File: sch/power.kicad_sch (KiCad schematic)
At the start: 3 parts

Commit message: Memory Module
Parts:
- removed C4: ~, Capacitor_THT:CP_Radial_D4.0mm_P1.50mm, symbol Device:C_Polarized_Small
- added C1: (no value), symbol Device:C_Polarized_Small
- added PWREG2: (no value), symbol Regulator_Linear:LT1962-5
- renumbered UPWR1 to PWREG1
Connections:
- net 5V: now also PWREG2.1 (OUT)
- net BOARD_IN: now also C3.1, PWREG1.1 (VIN), C1.1, PWREG2.8 (IN)
- net GND: now also C3.2, C1.2, PWREG2.4 (GND)
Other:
- moved on the sheet: C3, PWREG1
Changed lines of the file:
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@@
 (kicad_sch (version 20211123) (generator eeschema)
   (paper "A4")
-  (hierarchical_label "BOARD_IN" (shape input) (at 58.42 66.04 180)
+  (junction (at 139.7 114.3) (diameter 0) (color 0 0 0 0)
+  )
+  (junction (at 139.7 73.66) (diameter 0) (color 0 0 0 0)
+  )
+  (wire (pts (xy 139.7 73.66) (xy 139.7 78.74))
+    (stroke (width 0) (type default) (color 0 0 0 0))
+  )
+  (wire (pts (xy 177.8 114.3) (xy 165.1 114.3))
+    (stroke (width 0) (type default) (color 0 0 0 0))
+  )
+  (wire (pts (xy 139.7 114.3) (xy 144.78 114.3))
+    (stroke (width 0) (type default) (color 0 0 0 0))
+  )
+  (wire (pts (xy 127 73.66) (xy 139.7 73.66))
+    (stroke (width 0) (type default) (color 0 0 0 0))
+  )
+  (wire (pts (xy 139.7 114.3) (xy 139.7 119.38))
+    (stroke (width 0) (type default) (color 0 0 0 0))
+  )
+  (wire (pts (xy 127 114.3) (xy 139.7 114.3))
+    (stroke (width 0) (type default) (color 0 0 0 0))
+  )
+  (wire (pts (xy 139.7 73.66) (xy 144.78 73.66))
+    (stroke (width 0) (type default) (color 0 0 0 0))
+  )
+  (hierarchical_label "BOARD_IN" (shape input) (at 127 73.66 180)
     (effects (font (size 1.27 1.27)) (justify right))
   )
-  (hierarchical_label "3.3V" (shape output) (at 191.77 86.36 0)
+  (hierarchical_label "3.3V" (shape output) (at 191.77 83.82 0)
     (effects (font (size 1.27 1.27)) (justify left))
   )
-  (hierarchical_label "12V" (shape output) (at 191.77 78.74 0)
+  (hierarchical_label "12V" (shape output) (at 191.77 76.2 0)
     (effects (font (size 1.27 1.27)) (justify left))
   )
-  (hierarchical_label "5V" (shape output) (at 191.77 82.55 0)
+  (hierarchical_label "5V" (shape output) (at 177.8 114.3 0)
     (effects (font (size 1.27 1.27)) (justify left))
   )
-  (symbol (lib_id "Device:C_Polarized_Small") (at 86.36 68.58 0) (unit 1)
+  (hierarchical_label "BOARD_IN" (shape input) (at 127 114.3 180)
+    (effects (font (size 1.27 1.27)) (justify right))
+  )
+  (symbol (lib_id "power:GND") (at 154.94 127 0) (unit 1)
     (in_bom yes) (on_board yes) (fields_autoplaced)
-    (property "Reference" "C4" (id 0) (at 88.9 66.7638 0)
+    (property "Reference" "#PWR0117" (id 0) (at 154.94 133.35 0)
+      (effects (font (size 1.27 1.27)) hide)
+    )
+    (property "Value" "GND" (id 1) (at 154.94 132.08 0))
+    (property "Footprint" "" (id 2) (at 154.94 127 0)
+      (effects (font (size 1.27 1.27)) hide)
+    )
+    (property "Datasheet" "" (id 3) (at 154.94 127 0)
+      (effects (font (size 1.27 1.27)) hide)
+    )
+    (pin "1")
+  )
+  (symbol (lib_id "Device:C_Polarized_Small") (at 139.7 121.92 0) (unit 1)
+    (in_bom yes) (on_board yes)
+    (property "Reference" "C1" (id 0) (at 134.62 120.65 0)
       (effects (font (size 1.27 1.27)) (justify left))
     )
-    (property "Value" "~" (id 1) (at 88.9 69.3038 0)
+    (property "Value" "" (id 1) (at 119.38 123.19 0)
       (effects (font (size 1.27 1.27)) (justify left))
     )
-    (property "Footprint" "Capacitor_THT:CP_Radial_D4.0mm_P1.50mm" (id 2) (at 86.36 68.58 0)
+    (property "Footprint" "" (id 2) (at 139.7 121.92 0)
       (effects (font (size 1.27 1.27)) hide)
     )
-    (property "Datasheet" "~" (id 3) (at 86.36 68.58 0)
+    (property "Datasheet" "~" (id 3) (at 139.7 121.92 0)
       (effects (font (size 1.27 1.27)) hide)
     )
@@
     (pin "2")
   )
-  (symbol (lib_id "power:GND") (at 105.41 82.55 0) (unit 1)
+  (symbol (lib_id "power:GND") (at 154.94 83.82 0) (unit 1)
     (in_bom yes) (on_board yes) (fields_autoplaced)
-    (property "Reference" "#PWR01" (id 0) (at 105.41 88.9 0)
+    (property "Reference" "#PWR01" (id 0) (at 154.94 90.17 0)
       (effects (font (size 1.27 1.27)) hide)
     )
-    (property "Value" "GND" (id 1) (at 105.41 87.63 0))
-    (property "Footprint" "" (id 2) (at 105.41 82.55 0)
+    (property "Value" "GND" (id 1) (at 154.94 88.9 0))
+    (property "Footprint" "" (id 2) (at 154.94 83.82 0)
       (effects (font (size 1.27 1.27)) hide)
     )
-    (property "Datasheet" "" (id 3) (at 105.41 82.55 0)
+    (property "Datasheet" "" (id 3) (at 154.94 83.82 0)
       (effects (font (size 1.27 1.27)) hide)
     )
     (pin "1")
   )
-  (symbol (lib_id "Regulator_Linear:LT1761-1.5") (at 105.41 74.93 0) (unit 1)
+  (symbol (lib_id "Regulator_Linear:LT1962-5") (at 154.94 119.38 0) (unit 1)
     (in_bom yes) (on_board yes) (fields_autoplaced)
-    (property "Reference" "UPWR1" (id 0) (at 105.41 64.77 0))
-    (property "Value" "LT1761-1.5" (id 1) (at 105.41 67.31 0))
-    (property "Footprint" "Package_TO_SOT_SMD:TSOT-23-5" (id 2) (at 105.41 66.675 0)
+    (property "Reference" "PWREG2" (id 0) (at 154.94 106.68 0))
+    (property "Value" "" (id 1) (at 154.94 109.22 0))
+    (property "Footprint" "" (id 2) (at 154.94 128.27 0)
       (effects (font (size 1.27 1.27)) hide)
     )
-    (property "Datasheet" "https://www.analog.com/media/en/technical-documentation/data-sheets/1761sff.pdf" (id 3) (at 105.41 74.93 0)
+    (property "Datasheet" "https://www.analog.com/media/en/technical-documentation/data-sheets/1962fb.pdf" (id 3) (at 154.94 133.35 0)
+      (effects (font (size 1.27 1.27)) hide)
+    )
+    (pin "1")
+    (pin "2")
+    (pin "3")
+    (pin "4")
+    (pin "5")
+    (pin "6")
+    (pin "7")
+    (pin "8")
+  )
+  (symbol (lib_id "Regulator_Linear:LT1761-1.5") (at 154.94 76.2 0) (unit 1)
+    (in_bom yes) (on_board yes) (fields_autoplaced)
+    (property "Reference" "PWREG1" (id 0) (at 154.94 66.04 0))
+    (property "Value" "LT1761-1.5" (id 1) (at 154.94 68.58 0))
+    (property "Footprint" "Package_TO_SOT_SMD:TSOT-23-5" (id 2) (at 154.94 67.945 0)
+      (effects (font (size 1.27 1.27)) hide)
+    )
+    (property "Datasheet" "https://www.analog.com/media/en/technical-documentation/data-sheets/1761sff.pdf" (id 3) (at 154.94 76.2 0)
       (effects (font (size 1.27 1.27)) hide)
     )
@@
     (pin "5")
   )
-  (symbol (lib_id "Device:C_Polarized_Small") (at 90.17 58.42 0) (unit 1)
+  (symbol (lib_id "power:GND") (at 139.7 124.46 0) (unit 1)
+    (in_bom yes) (on_board yes) (fields_autoplaced)
+    (property "Reference" "#PWR0118" (id 0) (at 139.7 130.81 0)
+      (effects (font (size 1.27 1.27)) hide)
+    )
+    (property "Value" "GND" (id 1) (at 139.7 129.54 0))
+    (property "Footprint" "" (id 2) (at 139.7 124.46 0)
+      (effects (font (size 1.27 1.27)) hide)
+    )
+    (property "Datasheet" "" (id 3) (at 139.7 124.46 0)
+      (effects (font (size 1.27 1.27)) hide)
+    )
+    (pin "1")
+  )
+  (symbol (lib_id "power:GND") (at 139.7 83.82 0) (unit 1)
+    (in_bom yes) (on_board yes) (fields_autoplaced)
+    (property "Reference" "#PWR0111" (id 0) (at 139.7 90.17 0)
+      (effects (font (size 1.27 1.27)) hide)
+    )
+    (property "Value" "GND" (id 1) (at 139.7 88.9 0))
+    (property "Footprint" "" (id 2) (at 139.7 83.82 0)
+      (effects (font (size 1.27 1.27)) hide)
+    )
+    (property "Datasheet" "" (id 3) (at 139.7 83.82 0)
+      (effects (font (size 1.27 1.27)) hide)
+    )
+    (pin "1")
+  )
+  (symbol (lib_id "Device:C_Polarized_Small") (at 139.7 81.28 0) (unit 1)
     (in_bom yes) (on_board yes)
-    (property "Reference" "C3" (id 0) (at 92.71 56.6038 0)
+    (property "Reference" "C3" (id 0) (at 134.62 80.01 0)
       (effects (font (size 1.27 1.27)) (justify left))
     )
-    (property "Value" "C_Polarized_Small" (id 1) (at 92.71 59.1438 0)
+    (property "Value" "C_Polarized_Small" (id 1) (at 119.38 82.55 0)
       (effects (font (size 1.27 1.27)) (justify left))
     )
-    (property "Footprint" "Capacitor_THT:CP_Radial_D5.0mm_P2.00mm" (id 2) (at 90.17 58.42 0)
+    (property "Footprint" "Capacitor_THT:CP_Radial_D5.0mm_P2.00mm" (id 2) (at 139.7 81.28 0)
       (effects (font (size 1.27 1.27)) hide)
     )
-    (property "Datasheet" "~" (id 3) (at 90.17 58.42 0)
+    (property "Datasheet" "~" (id 3) (at 139.7 81.28 0)
       (effects (font (size 1.27 1.27)) hide)
     )

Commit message: Bus control
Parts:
- removed C3: C_Polarized_Small, Capacitor_THT:CP_Radial_D5.0mm_P2.00mm, symbol Device:C_Polarized_Small
- removed PWREG1: LT1761-1.5, Package_TO_SOT_SMD:TSOT-23-5, symbol Regulator_Linear:LT1761-1.5
- added C11: (no value), symbol Device:C
- added SW1: (no value), symbol Switch:SW_Push
- added U6: (no value), symbol Power_Supervisor:MAX811MEUS-T
- C1: footprint (none) -> Capacitor_THT:CP_Radial_D5.0mm_P2.00mm
- PWREG2: value (none) -> LT1962-5; footprint (none) -> Package_SO:MSOP-8_3x3mm_P0.65mm
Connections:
- net 5V: now also U6.4 (VCC)
- net GND: now also C11.2, SW1.1, U6.1 (GND)
- net BOARD_IN renamed PWR
- new net: C11.1, SW1.2, U6.3 (~{MR})
- new net RST: U6.2 (~{RESET})
- no-connect marks 0 -> 2
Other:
- moved on the sheet: C1, PWREG2

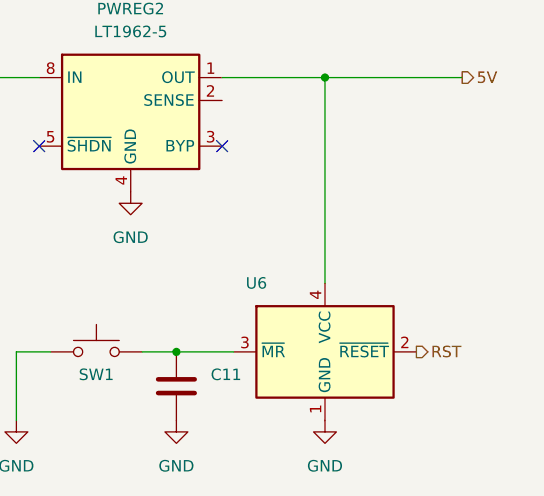
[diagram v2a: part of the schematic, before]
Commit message: New address decoder
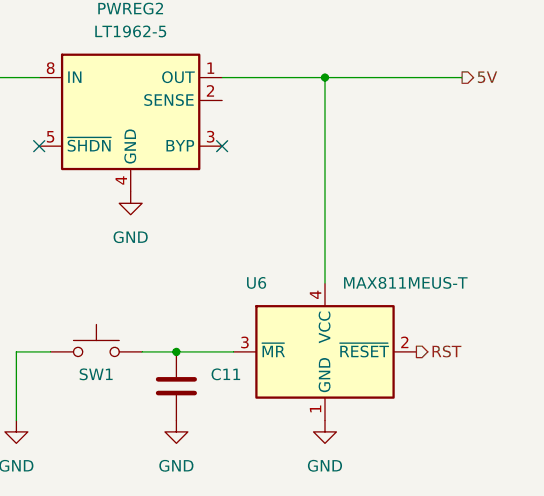
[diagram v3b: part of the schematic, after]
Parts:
- C1: footprint Capacitor_THT:CP_Radial_D5.0mm_P2.00mm -> (none)
- U6: value (none) -> MAX811MEUS-T; footprint (none) -> Package_TO_SOT_SMD:SOT-143
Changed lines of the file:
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@@
       (effects (font (size 1.27 1.27)) (justify right))
     )
-    (property "Footprint" "Capacitor_THT:CP_Radial_D5.0mm_P2.00mm" (id 2) (at 114.3 91.44 0)
+    (property "Footprint" "" (id 2) (at 114.3 91.44 0)
       (effects (font (size 1.27 1.27)) hide)
     )
@@
     (in_bom yes) (on_board yes)
     (property "Reference" "U6" (id 0) (at 148.59 104.14 0))
-    (property "Value" "" (id 1) (at 165.1 104.14 0))
-    (property "Footprint" "" (id 2) (at 158.75 119.38 0)
+    (property "Value" "MAX811MEUS-T" (id 1) (at 165.1 104.14 0))
+    (property "Footprint" "Package_TO_SOT_SMD:SOT-143" (id 2) (at 158.75 119.38 0)
       (effects (font (size 1.27 1.27)) (justify left) hide)
     )

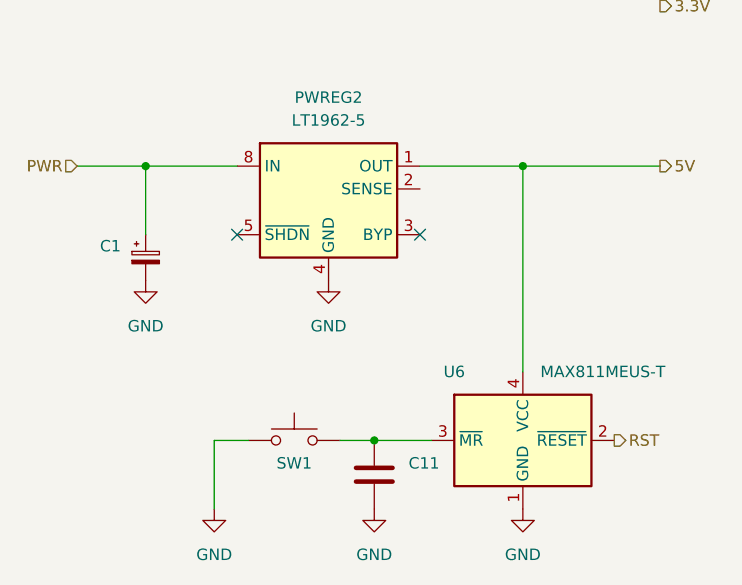
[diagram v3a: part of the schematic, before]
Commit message: Board layout, addr bus
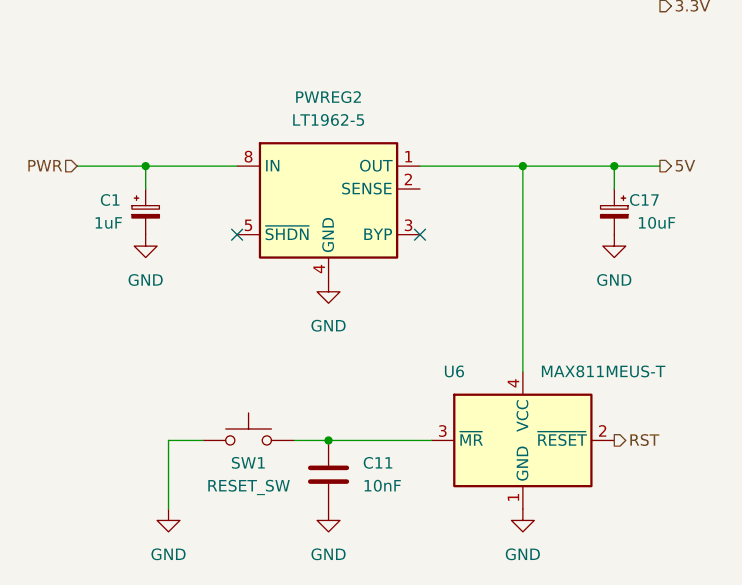
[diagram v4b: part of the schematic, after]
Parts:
- added C17: 10uF, Capacitor_THT:CP_Radial_D5.0mm_P2.00mm, symbol Device:C_Polarized_Small
- C1: value (none) -> 1uF; footprint (none) -> Capacitor_THT:CP_Radial_D5.0mm_P2.00mm
- C11: value (none) -> 10nF; footprint (none) -> Capacitor_SMD:C_1206_3216Metric_Pad1.33x1.80mm_HandSolder
- SW1: value (none) -> RESET_SW; footprint (none) -> Button_Switch_THT:SW_PUSH_6mm_H13mm
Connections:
- net 5V: now also C17.1
- net GND: now also C17.2
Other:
- moved on the sheet: C1, C11, SW1
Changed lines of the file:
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@@
   (junction (at 114.3 81.28) (diameter 0) (color 0 0 0 0)
   )
-  (junction (at 139.7 111.76) (diameter 0) (color 0 0 0 0)
+  (junction (at 166.37 81.28) (diameter 0) (color 0 0 0 0)
+  )
+  (junction (at 134.62 111.76) (diameter 0) (color 0 0 0 0)
   )
   (no_connect (at 124.46 88.9))
   (no_connect (at 144.78 88.9))
-  (wire (pts (xy 171.45 81.28) (xy 156.21 81.28))
+  (wire (pts (xy 171.45 81.28) (xy 166.37 81.28))
     (stroke (width 0) (type default) (color 0 0 0 0))
   )
@@
     (stroke (width 0) (type default) (color 0 0 0 0))
   )
-  (wire (pts (xy 135.89 111.76) (xy 139.7 111.76))
+  (wire (pts (xy 130.81 111.76) (xy 134.62 111.76))
+    (stroke (width 0) (type default) (color 0 0 0 0))
+  )
+  (wire (pts (xy 166.37 81.28) (xy 156.21 81.28))
     (stroke (width 0) (type default) (color 0 0 0 0))
   )
@@
     (stroke (width 0) (type default) (color 0 0 0 0))
   )
-  (wire (pts (xy 114.3 81.28) (xy 114.3 88.9))
-    (stroke (width 0) (type default) (color 0 0 0 0))
-  )
-  (wire (pts (xy 121.92 111.76) (xy 121.92 119.38))
+  (wire (pts (xy 114.3 81.28) (xy 114.3 83.82))
+    (stroke (width 0) (type default) (color 0 0 0 0))
+  )
+  (wire (pts (xy 116.84 111.76) (xy 116.84 119.38))
     (stroke (width 0) (type default) (color 0 0 0 0))
   )
@@
     (stroke (width 0) (type default) (color 0 0 0 0))
   )
-  (wire (pts (xy 125.73 111.76) (xy 121.92 111.76))
-    (stroke (width 0) (type default) (color 0 0 0 0))
-  )
-  (wire (pts (xy 139.7 111.76) (xy 146.05 111.76))
+  (wire (pts (xy 120.65 111.76) (xy 116.84 111.76))
+    (stroke (width 0) (type default) (color 0 0 0 0))
+  )
+  (wire (pts (xy 166.37 81.28) (xy 166.37 83.82))
+    (stroke (width 0) (type default) (color 0 0 0 0))
+  )
+  (wire (pts (xy 134.62 111.76) (xy 146.05 111.76))
     (stroke (width 0) (type default) (color 0 0 0 0))
   )
@@
     (pin "1")
   )
-  (symbol (lib_id "Device:C_Polarized_Small") (at 114.3 91.44 0) (unit 1)
-    (in_bom yes) (on_board yes)
-    (property "Reference" "C1" (id 0) (at 109.22 90.17 0)
-      (effects (font (size 1.27 1.27)) (justify left))
-    )
-    (property "Value" "" (id 1) (at 111.76 92.71 0)
+  (symbol (lib_id "Device:C_Polarized_Small") (at 114.3 86.36 0) (unit 1)
+    (in_bom yes) (on_board yes)
+    (property "Reference" "C1" (id 0) (at 109.22 85.09 0)
+      (effects (font (size 1.27 1.27)) (justify left))
+    )
+    (property "Value" "1uF" (id 1) (at 111.76 87.63 0)
       (effects (font (size 1.27 1.27)) (justify right))
     )
-    (property "Footprint" "" (id 2) (at 114.3 91.44 0)
-      (effects (font (size 1.27 1.27)) hide)
-    )
-    (property "Datasheet" "~" (id 3) (at 114.3 91.44 0)
+    (property "Footprint" "Capacitor_THT:CP_Radial_D5.0mm_P2.00mm" (id 2) (at 114.3 86.36 0)
+      (effects (font (size 1.27 1.27)) hide)
+    )
+    (property "Datasheet" "~" (id 3) (at 114.3 86.36 0)
       (effects (font (size 1.27 1.27)) hide)
     )
@@
     (pin "8")
   )
-  (symbol (lib_id "power:GND") (at 121.92 119.38 0) (unit 1)
-    (in_bom yes) (on_board yes) (fields_autoplaced)
-    (property "Reference" "#PWR0125" (id 0) (at 121.92 125.73 0)
-      (effects (font (size 1.27 1.27)) hide)
-    )
-    (property "Value" "GND" (id 1) (at 121.92 124.46 0))
-    (property "Footprint" "" (id 2) (at 121.92 119.38 0)
-      (effects (font (size 1.27 1.27)) hide)
-    )
-    (property "Datasheet" "" (id 3) (at 121.92 119.38 0)
-      (effects (font (size 1.27 1.27)) hide)
-    )
-    (pin "1")
-  )
-  (symbol (lib_id "Device:C") (at 139.7 115.57 0) (unit 1)
-    (in_bom yes) (on_board yes) (fields_autoplaced)
-    (property "Reference" "C11" (id 0) (at 143.51 114.2999 0)
-      (effects (font (size 1.27 1.27)) (justify left))
-    )
-    (property "Value" "" (id 1) (at 143.51 116.8399 0)
-      (effects (font (size 1.27 1.27)) (justify left))
-    )
-    (property "Footprint" "" (id 2) (at 140.6652 119.38 0)
-      (effects (font (size 1.27 1.27)) hide)
-    )
-    (property "Datasheet" "~" (id 3) (at 139.7 115.57 0)
-      (effects (font (size 1.27 1.27)) hide)
-    )
-    (pin "1")
-    (pin "2")
-  )
-  (symbol (lib_id "power:GND") (at 114.3 93.98 0) (unit 1)
-    (in_bom yes) (on_board yes) (fields_autoplaced)
-    (property "Reference" "#PWR0118" (id 0) (at 114.3 100.33 0)
-      (effects (font (size 1.27 1.27)) hide)
-    )
-    (property "Value" "GND" (id 1) (at 114.3 99.06 0))
-    (property "Footprint" "" (id 2) (at 114.3 93.98 0)
-      (effects (font (size 1.27 1.27)) hide)
-    )
-    (property "Datasheet" "" (id 3) (at 114.3 93.98 0)
+  (symbol (lib_id "power:GND") (at 116.84 119.38 0) (unit 1)
+    (in_bom yes) (on_board yes) (fields_autoplaced)
+    (property "Reference" "#PWR0125" (id 0) (at 116.84 125.73 0)
+      (effects (font (size 1.27 1.27)) hide)
+    )
+    (property "Value" "GND" (id 1) (at 116.84 124.46 0))
+    (property "Footprint" "" (id 2) (at 116.84 119.38 0)
+      (effects (font (size 1.27 1.27)) hide)
+    )
+    (property "Datasheet" "" (id 3) (at 116.84 119.38 0)
+      (effects (font (size 1.27 1.27)) hide)
+    )
+    (pin "1")
+  )
+  (symbol (lib_id "Device:C") (at 134.62 115.57 0) (unit 1)
+    (in_bom yes) (on_board yes) (fields_autoplaced)
+    (property "Reference" "C11" (id 0) (at 138.43 114.2999 0)
+      (effects (font (size 1.27 1.27)) (justify left))
+    )
+    (property "Value" "10nF" (id 1) (at 138.43 116.8399 0)
+      (effects (font (size 1.27 1.27)) (justify left))
+    )
+    (property "Footprint" "Capacitor_SMD:C_1206_3216Metric_Pad1.33x1.80mm_HandSolder" (id 2) (at 135.5852 119.38 0)
+      (effects (font (size 1.27 1.27)) hide)
+    )
+    (property "Datasheet" "~" (id 3) (at 134.62 115.57 0)
+      (effects (font (size 1.27 1.27)) hide)
+    )
+    (pin "1")
+    (pin "2")
+  )
+  (symbol (lib_id "power:GND") (at 114.3 88.9 0) (unit 1)
+    (in_bom yes) (on_board yes) (fields_autoplaced)
+    (property "Reference" "#PWR0118" (id 0) (at 114.3 95.25 0)
+      (effects (font (size 1.27 1.27)) hide)
+    )
+    (property "Value" "GND" (id 1) (at 114.3 93.98 0))
+    (property "Footprint" "" (id 2) (at 114.3 88.9 0)
+      (effects (font (size 1.27 1.27)) hide)
+    )
+    (property "Datasheet" "" (id 3) (at 114.3 88.9 0)
       (effects (font (size 1.27 1.27)) hide)
     )
@@
     (pin "4")
   )
-  (symbol (lib_id "power:GND") (at 139.7 119.38 0) (unit 1)
-    (in_bom yes) (on_board yes) (fields_autoplaced)
-    (property "Reference" "#PWR0124" (id 0) (at 139.7 125.73 0)
-      (effects (font (size 1.27 1.27)) hide)
-    )
-    (property "Value" "GND" (id 1) (at 139.7 124.46 0))
-    (property "Footprint" "" (id 2) (at 139.7 119.38 0)
-      (effects (font (size 1.27 1.27)) hide)
-    )
-    (property "Datasheet" "" (id 3) (at 139.7 119.38 0)
-      (effects (font (size 1.27 1.27)) hide)
-    )
-    (pin "1")
-  )
-  (symbol (lib_id "Switch:SW_Push") (at 130.81 111.76 0) (unit 1)
-    (in_bom yes) (on_board yes)
-    (property "Reference" "SW1" (id 0) (at 130.81 114.3 0))
-    (property "Value" "" (id 1) (at 130.81 116.84 0))
-    (property "Footprint" "" (id 2) (at 130.81 106.68 0)
-      (effects (font (size 1.27 1.27)) hide)
-    )
-    (property "Datasheet" "~" (id 3) (at 130.81 106.68 0)
-      (effects (font (size 1.27 1.27)) hide)
-    )
+  (symbol (lib_id "power:GND") (at 134.62 119.38 0) (unit 1)
+    (in_bom yes) (on_board yes) (fields_autoplaced)
+    (property "Reference" "#PWR0124" (id 0) (at 134.62 125.73 0)
+      (effects (font (size 1.27 1.27)) hide)
+    )
+    (property "Value" "GND" (id 1) (at 134.62 124.46 0))
+    (property "Footprint" "" (id 2) (at 134.62 119.38 0)
+      (effects (font (size 1.27 1.27)) hide)
+    )
+    (property "Datasheet" "" (id 3) (at 134.62 119.38 0)
+      (effects (font (size 1.27 1.27)) hide)
+    )
+    (pin "1")
+  )
+  (symbol (lib_id "Switch:SW_Push") (at 125.73 111.76 0) (unit 1)
+    (in_bom yes) (on_board yes)
+    (property "Reference" "SW1" (id 0) (at 125.73 114.3 0))
+    (property "Value" "RESET_SW" (id 1) (at 125.73 116.84 0))
+    (property "Footprint" "Button_Switch_THT:SW_PUSH_6mm_H13mm" (id 2) (at 125.73 106.68 0)
+      (effects (font (size 1.27 1.27)) hide)
+    )
+    (property "Datasheet" "~" (id 3) (at 125.73 106.68 0)
+      (effects (font (size 1.27 1.27)) hide)
+    )
+    (pin "1")
+    (pin "2")
+  )
+  (symbol (lib_id "power:GND") (at 166.37 88.9 0) (unit 1)
+    (in_bom yes) (on_board yes) (fields_autoplaced)
+    (property "Reference" "#PWR0126" (id 0) (at 166.37 95.25 0)
+      (effects (font (size 1.27 1.27)) hide)
+    )
+    (property "Value" "GND" (id 1) (at 166.37 93.98 0))
+    (property "Footprint" "" (id 2) (at 166.37 88.9 0)
+      (effects (font (size 1.27 1.27)) hide)
+    )
+    (property "Datasheet" "" (id 3) (at 166.37 88.9 0)
+      (effects (font (size 1.27 1.27)) hide)
+    )
+    (pin "1")
+  )
+  (symbol (lib_id "Device:C_Polarized_Small") (at 166.37 86.36 0) (mirror y) (unit 1)
+    (in_bom yes) (on_board yes)
+    (property "Reference" "C17" (id 0) (at 171.45 85.09 0)
+      (effects (font (size 1.27 1.27)) (justify left))
+    )
+    (property "Value" "10uF" (id 1) (at 168.91 87.63 0)
+      (effects (font (size 1.27 1.27)) (justify right))
+    )
+    (property "Footprint" "Capacitor_THT:CP_Radial_D5.0mm_P2.00mm" (id 2) (at 166.37 86.36 0)
+      (effects (font (size 1.27 1.27)) hide)
+    )
+    (property "Datasheet" "~" (id 3) (at 166.37 86.36 0)
+      (effects (font (size 1.27 1.27)) hide)
+    )
